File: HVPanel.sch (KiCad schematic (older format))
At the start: 5 parts

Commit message: almost done!
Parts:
- added B+ (x2), B- (x2): Conn_01x01, symbol Conn_01x01
- added FUSING, FUSING2: LTO100, symbol Fuse
- added JP2: Conn_01x08, symbol Conn_01x08
- added U$3: AMPSEAL14, symbol Conn_01x14
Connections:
- net labels added: B+, B-, CHASSIS_GND, CHASSIS_GND2, D_OUT_HIGH, D_OUT_LOW, GLV_GND, HV+, HV+2, HV-, HV-2, IMD+, IMD-, IMD_FAULT, IMD_SUPPLY
- wire segments 16 -> 37
- no-connect marks 0 -> 5
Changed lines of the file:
@@
 Wire Wire Line
 	2850 3100 2850 3450
+$Comp
+L GND #PWR?
+U 1 1 5A2EC229
+P 2850 3100
+F 0 "#PWR?" H 2850 2850 50  0001 C CNN
+F 1 "GND" H 2850 2950 50  0000 C CNN
+F 2 "" H 2850 3100 50  0001 C CNN
+F 3 "" H 2850 3100 50  0001 C CNN
+	1    2850 3100
+	-1   0    0    1
+$EndComp
+Text Label 2850 3050 0    60   ~ 0
+GLV_GND
+Text Label 2850 3450 0    60   ~ 0
+CHASSIS_GND
+Wire Wire Line
+	2500 3000 2500 2750
+Wire Wire Line
+	2200 3000 2200 2750
+$Comp
+L Fuse FUSING2
+U 1 1 5A2EC41C
+P 2500 3150
+F 0 "FUSING2" V 2580 3150 50  0000 C CNN
+F 1 "LTO100" V 2425 3150 50  0000 C CNN
+F 2 "" V 2430 3150 50  0001 C CNN
+F 3 "" H 2500 3150 50  0001 C CNN
+	1    2500 3150
+	1    0    0    -1
+$EndComp
+$Comp
+L Fuse FUSING
+U 1 1 5A2EC47F
+P 2200 3150
+F 0 "FUSING" V 2280 3150 50  0000 C CNN
+F 1 "LTO100" V 2125 3150 50  0000 C CNN
+F 2 "" V 2130 3150 50  0001 C CNN
+F 3 "" H 2200 3150 50  0001 C CNN
+	1    2200 3150
+	1    0    0    -1
+$EndComp
+Wire Wire Line
+	2500 3300 2500 3450
+Wire Wire Line
+	2200 3300 2200 3450
+$Comp
+L Conn_01x01 B-
+U 1 1 5A2EC6F3
+P 2500 3650
+F 0 "B-" H 2500 3750 50  0000 C CNN
+F 1 "Conn_01x01" H 2500 3550 50  0000 C CNN
+F 2 "" H 2500 3650 50  0001 C CNN
+F 3 "" H 2500 3650 50  0001 C CNN
+	1    2500 3650
+	0    1    1    0
+$EndComp
+$Comp
+L Conn_01x01 B+
+U 1 1 5A2EC75B
+P 2200 3650
+F 0 "B+" H 2200 3750 50  0000 C CNN
+F 1 "Conn_01x01" H 2200 3550 50  0000 C CNN
+F 2 "" H 2200 3650 50  0001 C CNN
+F 3 "" H 2200 3650 50  0001 C CNN
+	1    2200 3650
+	0    1    1    0
+$EndComp
+Text Label 2500 2650 3    60   ~ 0
+B-
+Text Label 2600 2800 1    60   ~ 0
+HV-
+Text Label 2200 2800 1    60   ~ 0
+B+
+Text Label 2300 2800 1    60   ~ 0
+HV+
+Wire Wire Line
+	2500 3950 2500 4400
+Wire Wire Line
+	2200 3950 2200 4250
+NoConn ~ 2500 3950
+NoConn ~ 2200 3950
+NoConn ~ 2500 2750
+NoConn ~ 2200 2750
+NoConn ~ 2850 3050
+$Comp
+L Conn_01x01 B-
+U 1 1 5A2ECB68
+P 2500 4600
+F 0 "B-" H 2500 4700 50  0000 C CNN
+F 1 "Conn_01x01" H 2500 4500 50  0000 C CNN
+F 2 "" H 2500 4600 50  0001 C CNN
+F 3 "" H 2500 4600 50  0001 C CNN
+	1    2500 4600
+	0    1    1    0
+$EndComp
+$Comp
+L Conn_01x01 B+
+U 1 1 5A2ECBA0
+P 2200 4450
+F 0 "B+" H 2200 4550 50  0000 C CNN
+F 1 "Conn_01x01" H 2200 4350 50  0000 C CNN
+F 2 "" H 2200 4450 50  0001 C CNN
+F 3 "" H 2200 4450 50  0001 C CNN
+	1    2200 4450
+	0    1    1    0
+$EndComp
+Text Label 2600 4150 1    60   ~ 0
+HV-2
+Text Label 2500 4150 1    60   ~ 0
+IMD-
+Text Label 2300 4150 1    60   ~ 0
+HV+2
+Text Label 2200 4150 1    60   ~ 0
+IMD+
+$Comp
+L Conn_01x14 U$3
+U 1 1 5A2ED351
+P 7200 3400
+F 0 "U$3" H 7200 4100 50  0000 C CNN
+F 1 "AMPSEAL14" H 7200 2600 50  0000 C CNN
+F 2 "" H 7200 3400 50  0001 C CNN
+F 3 "" H 7200 3400 50  0001 C CNN
+	1    7200 3400
+	1    0    0    -1
+$EndComp
+Wire Wire Line
+	7000 3500 6800 3500
+Wire Wire Line
+	7000 3600 6800 3600
+Wire Wire Line
+	7000 2800 6800 2800
+Wire Wire Line
+	7000 2900 6800 2900
+Wire Wire Line
+	7000 3000 6800 3000
+Wire Wire Line
+	7000 3100 6800 3100
+Wire Wire Line
+	7000 3200 6800 3200
+Wire Wire Line
+	7000 3300 6800 3300
+Wire Wire Line
+	7000 3400 6800 3400
+Text Label 6700 2800 0    60   ~ 0
+TSEL+
+Text Label 6400 2900 0    60   ~ 0
+IMD_SUPPLY
+Text Label 6300 3000 0    60   ~ 0
+CHASSIS_GND2
+Text Label 6400 3100 0    60   ~ 0
+D_OUT_LOW
+Text Label 6450 3200 0    60   ~ 0
+IMD_FAULT
+Text Label 6700 3300 0    60   ~ 0
+GND
+Text Label 6350 3400 0    60   ~ 0
+CHASSIS_GND
+Text Label 6400 3500 0    60   ~ 0
+D_OUT_HIGH
+Text Label 6700 3600 0    60   ~ 0
+TSEL-
+$Comp
+L Conn_01x08 JP2
+U 1 1 5A2EDCE2
+P 4900 1800
+F 0 "JP2" H 4900 2200 50  0000 C CNN
+F 1 "Conn_01x08" H 4900 1300 50  0000 C CNN
+F 2 "" H 4900 1800 50  0001 C CNN
+F 3 "" H 4900 1800 50  0001 C CNN
+	1    4900 1800
+	1    0    0    -1
+$EndComp
+Wire Wire Line
+	4700 1500 4500 1500
+Wire Wire Line
+	4700 1600 4500 1600
+Wire Wire Line
+	4700 1700 4500 1700
+Wire Wire Line
+	4700 1900 4500 1900
+Wire Wire Line
+	4700 2000 4500 2000
+Wire Wire Line
+	4700 2200 4500 2200
 $EndSCHEMATC

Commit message: finished schematic
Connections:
- wire segments 37 -> 38
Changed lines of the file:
@@
 Wire Wire Line
 	4700 2200 4500 2200
+Text Label 4150 2200 0    60   ~ 0
+IMD_FAULT
+Text Label 4400 1500 0    60   ~ 0
+GND
+Text Label 4050 1600 0    60   ~ 0
+IMD_SUPPLY
+Text Label 4000 1700 0    60   ~ 0
+CHASSIS_GND
+Wire Wire Line
+	4700 1800 4500 1800
+Text Label 3950 1800 0    60   ~ 0
+CHASSIS_GND2
+Text Label 4100 1900 0    60   ~ 0
+D_OUT_HIGH
+Text Label 4100 2000 0    60   ~ 0
+D_OUT_LOW
 $EndSCHEMATC

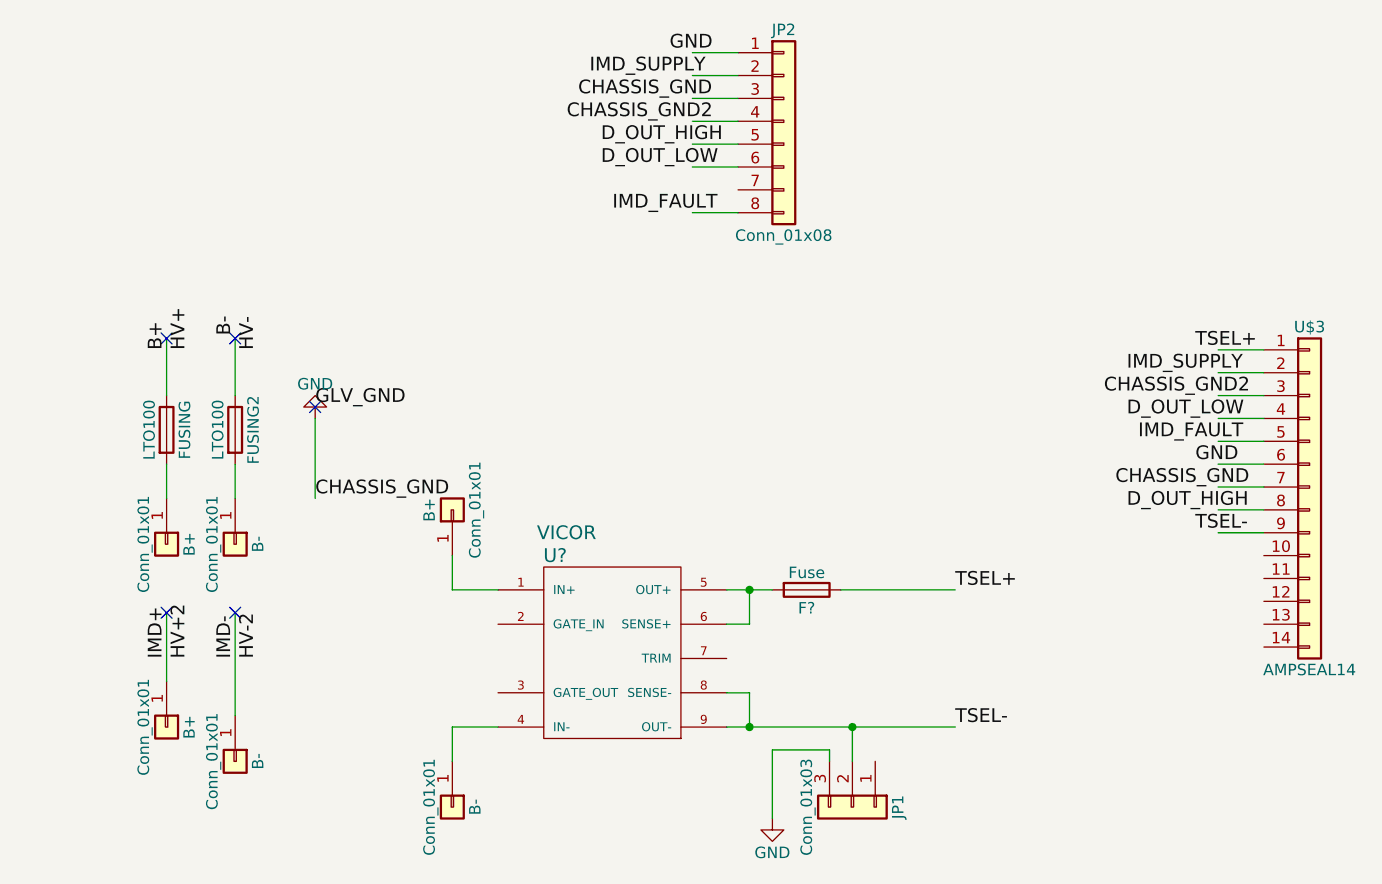
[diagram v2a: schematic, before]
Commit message: started footprint
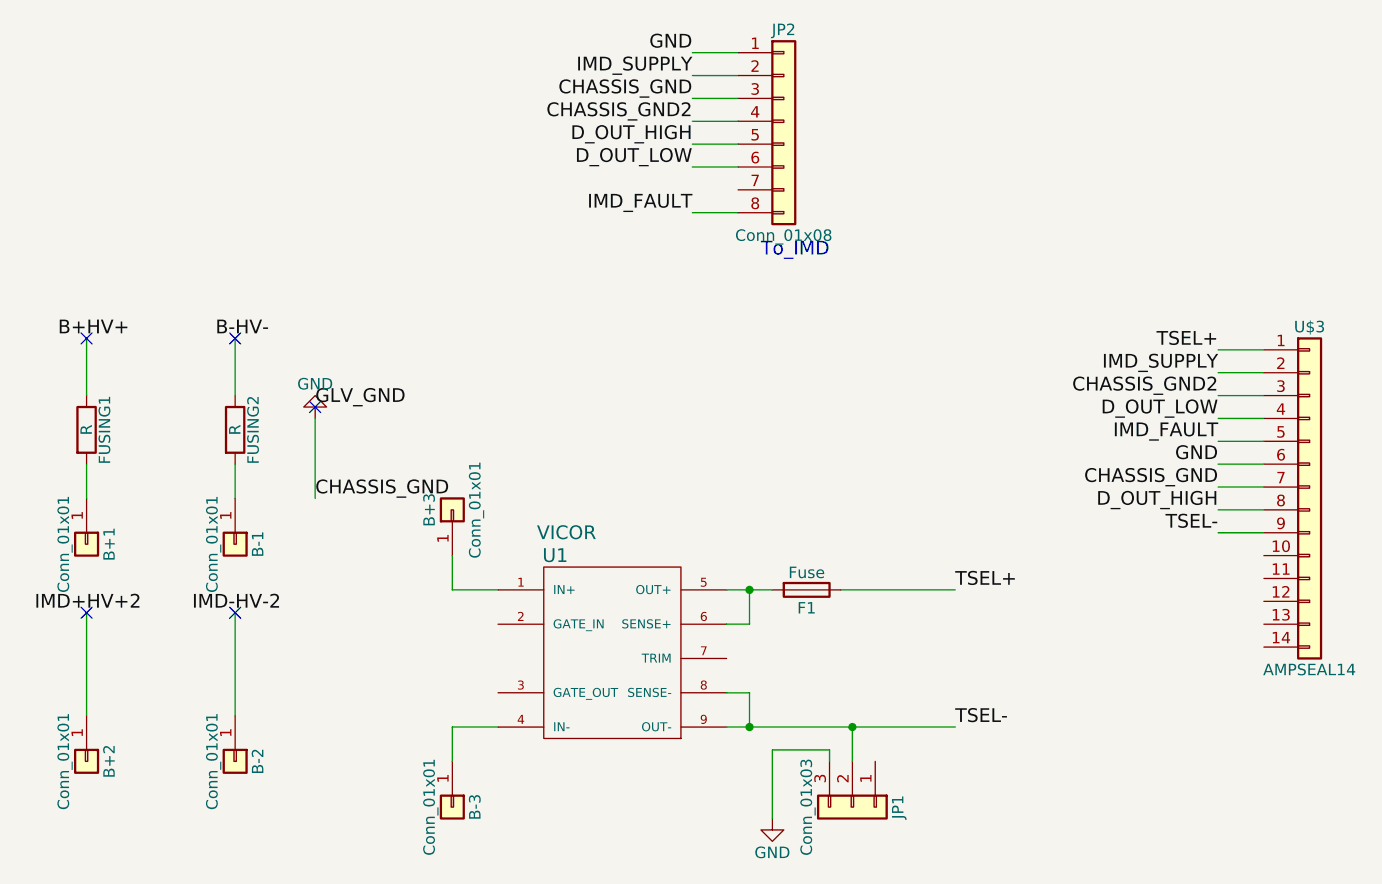
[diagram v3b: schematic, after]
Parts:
- removed FUSING, FUSING2: LTO100, symbol Fuse
- added FUSING1, FUSING2: R, TO_SOT_Packages_THT:TO-247-2_Vertical, symbol R
- B+1, B+2, B+3: renamed from B+; footprint (none) -> Wire_Pads:SolderWirePad_single_1-5mmDrill
- B-1, B-2, B-3: renamed from B-; footprint (none) -> Wire_Pads:SolderWirePad_single_1-5mmDrill
- U$3: footprint (none) -> TuftsRacing2018:AMP14
- gave numbers to parts that had none: 2
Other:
- note added: "To_IMD"
- moved on the sheet: B+1, B+2
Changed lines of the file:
@@
 $EndDescr
 $Comp
-L VICOR U?
+L VICOR U1
 U 1 1 5A1C5270
 P 4000 3800
-F 0 "U?" H 3900 3900 60  0000 C CNN
+F 0 "U1" H 3900 3900 60  0000 C CNN
 F 1 "VICOR" H 3950 4000 60  0000 C CNN
 F 2 "" H 4000 3750 60  0001 C CNN
@@
 Connection ~ 4750 4450
 $Comp
-L Fuse F?
+L Fuse F1
 U 1 1 5A282BE3
 P 5000 3850
-F 0 "F?" V 5080 3850 50  0000 C CNN
+F 0 "F1" V 5080 3850 50  0000 C CNN
 F 1 "Fuse" V 4925 3850 50  0000 C CNN
 F 2 "" V 4930 3850 50  0001 C CNN
@@
 $EndComp
 $Comp
-L Conn_01x01 B+
+L Conn_01x01 B+3
 U 1 1 5A282C6A
 P 3450 3500
-F 0 "B+" H 3450 3600 50  0000 C CNN
+F 0 "B+3" H 3450 3600 50  0000 C CNN
 F 1 "Conn_01x01" H 3450 3400 50  0000 C CNN
-F 2 "" H 3450 3500 50  0001 C CNN
+F 2 "Wire_Pads:SolderWirePad_single_1-5mmDrill" H 3450 3500 50  0001 C CNN
 F 3 "" H 3450 3500 50  0001 C CNN
 	1    3450 3500
@@
 $EndComp
 $Comp
-L Conn_01x01 B-
+L Conn_01x01 B-3
 U 1 1 5A282CDC
 P 3450 4800
-F 0 "B-" H 3450 4900 50  0000 C CNN
+F 0 "B-3" H 3450 4900 50  0000 C CNN
 F 1 "Conn_01x01" H 3450 4700 50  0000 C CNN
-F 2 "" H 3450 4800 50  0001 C CNN
+F 2 "Wire_Pads:SolderWirePad_single_1-5mmDrill" H 3450 4800 50  0001 C CNN
 F 3 "" H 3450 4800 50  0001 C CNN
 	1    3450 4800
@@
 	4850 4550 4850 4850
 $Comp
-L GND #PWR?
+L GND #PWR01
 U 1 1 5A282F5C
 P 4850 4850
-F 0 "#PWR?" H 4850 4600 50  0001 C CNN
+F 0 "#PWR01" H 4850 4600 50  0001 C CNN
 F 1 "GND" H 4850 4700 50  0000 C CNN
 F 2 "" H 4850 4850 50  0001 C CNN
@@
 	2850 3100 2850 3450
 $Comp
-L GND #PWR?
+L GND #PWR02
 U 1 1 5A2EC229
 P 2850 3100
-F 0 "#PWR?" H 2850 2850 50  0001 C CNN
+F 0 "#PWR02" H 2850 2850 50  0001 C CNN
 F 1 "GND" H 2850 2950 50  0000 C CNN
 F 2 "" H 2850 3100 50  0001 C CNN
@@
 	2500 3000 2500 2750
 Wire Wire Line
-	2200 3000 2200 2750
-$Comp
-L Fuse FUSING2
-U 1 1 5A2EC41C
-P 2500 3150
-F 0 "FUSING2" V 2580 3150 50  0000 C CNN
-F 1 "LTO100" V 2425 3150 50  0000 C CNN
-F 2 "" V 2430 3150 50  0001 C CNN
-F 3 "" H 2500 3150 50  0001 C CNN
-	1    2500 3150
-	1    0    0    -1
-$EndComp
-$Comp
-L Fuse FUSING
-U 1 1 5A2EC47F
-P 2200 3150
-F 0 "FUSING" V 2280 3150 50  0000 C CNN
-F 1 "LTO100" V 2125 3150 50  0000 C CNN
-F 2 "" V 2130 3150 50  0001 C CNN
-F 3 "" H 2200 3150 50  0001 C CNN
-	1    2200 3150
-	1    0    0    -1
-$EndComp
-Wire Wire Line
 	2500 3300 2500 3450
-Wire Wire Line
-	2200 3300 2200 3450
-$Comp
-L Conn_01x01 B-
+$Comp
+L Conn_01x01 B-1
 U 1 1 5A2EC6F3
 P 2500 3650
-F 0 "B-" H 2500 3750 50  0000 C CNN
+F 0 "B-1" H 2500 3750 50  0000 C CNN
 F 1 "Conn_01x01" H 2500 3550 50  0000 C CNN
-F 2 "" H 2500 3650 50  0001 C CNN
+F 2 "Wire_Pads:SolderWirePad_single_1-5mmDrill" H 2500 3650 50  0001 C CNN
 F 3 "" H 2500 3650 50  0001 C CNN
 	1    2500 3650
@@
 $EndComp
 $Comp
-L Conn_01x01 B+
+L Conn_01x01 B+1
 U 1 1 5A2EC75B
-P 2200 3650
-F 0 "B+" H 2200 3750 50  0000 C CNN
-F 1 "Conn_01x01" H 2200 3550 50  0000 C CNN
-F 2 "" H 2200 3650 50  0001 C CNN
-F 3 "" H 2200 3650 50  0001 C CNN
-	1    2200 3650
-	0    1    1    0
-$EndComp
-Text Label 2500 2650 3    60   ~ 0
+P 1850 3650
+F 0 "B+1" H 1850 3750 50  0000 C CNN
+F 1 "Conn_01x01" H 1850 3550 50  0000 C CNN
+F 2 "Wire_Pads:SolderWirePad_single_1-5mmDrill" H 1850 3650 50  0001 C CNN
+F 3 "" H 1850 3650 50  0001 C CNN
+	1    1850 3650
+	0    1    1    0
+$EndComp
+Text Label 2500 2750 2    60   ~ 0
 B-
-Text Label 2600 2800 1    60   ~ 0
+Text Label 2500 2750 0    60   ~ 0
 HV-
-Text Label 2200 2800 1    60   ~ 0
+Text Label 1850 2750 2    60   ~ 0
 B+
-Text Label 2300 2800 1    60   ~ 0
+Text Label 1850 2750 0    60   ~ 0
 HV+
 Wire Wire Line
 	2500 3950 2500 4400
-Wire Wire Line
-	2200 3950 2200 4250
 NoConn ~ 2500 3950
-NoConn ~ 2200 3950
 NoConn ~ 2500 2750
-NoConn ~ 2200 2750
 NoConn ~ 2850 3050
 $Comp
-L Conn_01x01 B-
+L Conn_01x01 B-2
 U 1 1 5A2ECB68
 P 2500 4600
-F 0 "B-" H 2500 4700 50  0000 C CNN
+F 0 "B-2" H 2500 4700 50  0000 C CNN
 F 1 "Conn_01x01" H 2500 4500 50  0000 C CNN
-F 2 "" H 2500 4600 50  0001 C CNN
+F 2 "Wire_Pads:SolderWirePad_single_1-5mmDrill" H 2500 4600 50  0001 C CNN
 F 3 "" H 2500 4600 50  0001 C CNN
 	1    2500 4600
@@
 $EndComp
 $Comp
-L Conn_01x01 B+
+L Conn_01x01 B+2
 U 1 1 5A2ECBA0
-P 2200 4450
-F 0 "B+" H 2200 4550 50  0000 C CNN
-F 1 "Conn_01x01" H 2200 4350 50  0000 C CNN
-F 2 "" H 2200 4450 50  0001 C CNN
-F 3 "" H 2200 4450 50  0001 C CNN
-	1    2200 4450
-	0    1    1    0
-$EndComp
-Text Label 2600 4150 1    60   ~ 0
+P 1850 4600
+F 0 "B+2" H 1850 4700 50  0000 C CNN
+F 1 "Conn_01x01" H 1850 4500 50  0000 C CNN
+F 2 "Wire_Pads:SolderWirePad_single_1-5mmDrill" H 1850 4600 50  0001 C CNN
+F 3 "" H 1850 4600 50  0001 C CNN
+	1    1850 4600
+	0    1    1    0
+$EndComp
+Text Label 2500 3950 0    60   ~ 0
 HV-2
-Text Label 2500 4150 1    60   ~ 0
+Text Label 2500 3950 2    60   ~ 0
 IMD-
-Text Label 2300 4150 1    60   ~ 0
+Text Label 1850 3950 0    60   ~ 0
 HV+2
-Text Label 2200 4150 1    60   ~ 0
+Text Label 1850 3950 2    60   ~ 0
 IMD+
 $Comp
@@
 F 0 "U$3" H 7200 4100 50  0000 C CNN
 F 1 "AMPSEAL14" H 7200 2600 50  0000 C CNN
-F 2 "" H 7200 3400 50  0001 C CNN
+F 2 "TuftsRacing2018:AMP14" H 7200 3400 50  0001 C CNN
 F 3 "" H 7200 3400 50  0001 C CNN
 	1    7200 3400
@@
 Wire Wire Line
 	7000 3400 6800 3400
-Text Label 6700 2800 0    60   ~ 0
+Text Label 6800 2800 2    60   ~ 0
 TSEL+
-Text Label 6400 2900 0    60   ~ 0
+Text Label 6800 2900 2    60   ~ 0
 IMD_SUPPLY
-Text Label 6300 3000 0    60   ~ 0
+Text Label 6800 3000 2    60   ~ 0
 CHASSIS_GND2
-Text Label 6400 3100 0    60   ~ 0
+Text Label 6800 3100 2    60   ~ 0
 D_OUT_LOW
-Text Label 6450 3200 0    60   ~ 0
+Text Label 6800 3200 2    60   ~ 0
 IMD_FAULT
-Text Label 6700 3300 0    60   ~ 0
+Text Label 6800 3300 2    60   ~ 0
 GND
-Text Label 6350 3400 0    60   ~ 0
+Text Label 6800 3400 2    60   ~ 0
 CHASSIS_GND
-Text Label 6400 3500 0    60   ~ 0
+Text Label 6800 3500 2    60   ~ 0
 D_OUT_HIGH
-Text Label 6700 3600 0    60   ~ 0
+Text Label 6800 3600 2    60   ~ 0
 TSEL-
 $Comp
@@
 Wire Wire Line
 	4700 2200 4500 2200
-Text Label 4150 2200 0    60   ~ 0
+Text Label 4500 2200 2    60   ~ 0
 IMD_FAULT
-Text Label 4400 1500 0    60   ~ 0
+Text Label 4500 1500 2    60   ~ 0
 GND
-Text Label 4050 1600 0    60   ~ 0
+Text Label 4500 1600 2    60   ~ 0
 IMD_SUPPLY
-Text Label 4000 1700 0    60   ~ 0
+Text Label 4500 1700 2    60   ~ 0
 CHASSIS_GND
 Wire Wire Line
 	4700 1800 4500 1800
-Text Label 3950 1800 0    60   ~ 0
+Text Label 4500 1800 2    60   ~ 0
 CHASSIS_GND2
-Text Label 4100 1900 0    60   ~ 0
+Text Label 4500 1900 2    60   ~ 0
 D_OUT_HIGH
-Text Label 4100 2000 0    60   ~ 0
+Text Label 4500 2000 2    60   ~ 0
 D_OUT_LOW
+Wire Wire Line
+	1850 3450 1850 3300
+Wire Wire Line
+	1850 3000 1850 2750
+NoConn ~ 1850 2750
+Wire Wire Line
+	1850 4400 1850 3950
+NoConn ~ 1850 3950
+Text Notes 4800 2400 0    60   ~ 0
+To_IMD
+$Comp
+L R FUSING1
+U 1 1 5A664BC1
+P 1850 3150
+F 0 "FUSING1" V 1930 3150 50  0000 C CNN
+F 1 "R" V 1850 3150 50  0000 C CNN
+F 2 "TO_SOT_Packages_THT:TO-247-2_Vertical" V 1780 3150 50  0001 C CNN
+F 3 "" H 1850 3150 50  0001 C CNN
+	1    1850 3150
+	1    0    0    -1
+$EndComp
+$Comp
+L R FUSING2
+U 1 1 5A664C34
+P 2500 3150
+F 0 "FUSING2" V 2580 3150 50  0000 C CNN
+F 1 "R" V 2500 3150 50  0000 C CNN
+F 2 "TO_SOT_Packages_THT:TO-247-2_Vertical" V 2430 3150 50  0001 C CNN
+F 3 "" H 2500 3150 50  0001 C CNN
+	1    2500 3150
+	1    0    0    -1
+$EndComp
 $EndSCHEMATC

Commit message: more footprint conversion
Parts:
- F1: footprint (none) -> Fuse_Holders_and_Fuses:BladeFuse-Mini_Keystone_3568
- U1: footprint (none) -> TuftsRacing2018:VICOR
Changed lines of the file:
@@
 F 0 "U1" H 3900 3900 60  0000 C CNN
 F 1 "VICOR" H 3950 4000 60  0000 C CNN
-F 2 "" H 4000 3750 60  0001 C CNN
+F 2 "TuftsRacing2018:VICOR" H 4000 3750 60  0001 C CNN
 F 3 "" H 4000 3750 60  0001 C CNN
 	1    4000 3800
@@
 F 0 "F1" V 5080 3850 50  0000 C CNN
 F 1 "Fuse" V 4925 3850 50  0000 C CNN
-F 2 "" V 4930 3850 50  0001 C CNN
+F 2 "Fuse_Holders_and_Fuses:BladeFuse-Mini_Keystone_3568" V 4930 3850 50  0001 C CNN
 F 3 "" H 5000 3850 50  0001 C CNN
 	1    5000 3850
